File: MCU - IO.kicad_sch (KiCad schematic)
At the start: 1 part, among them U1 STM32H743ZIT6TR

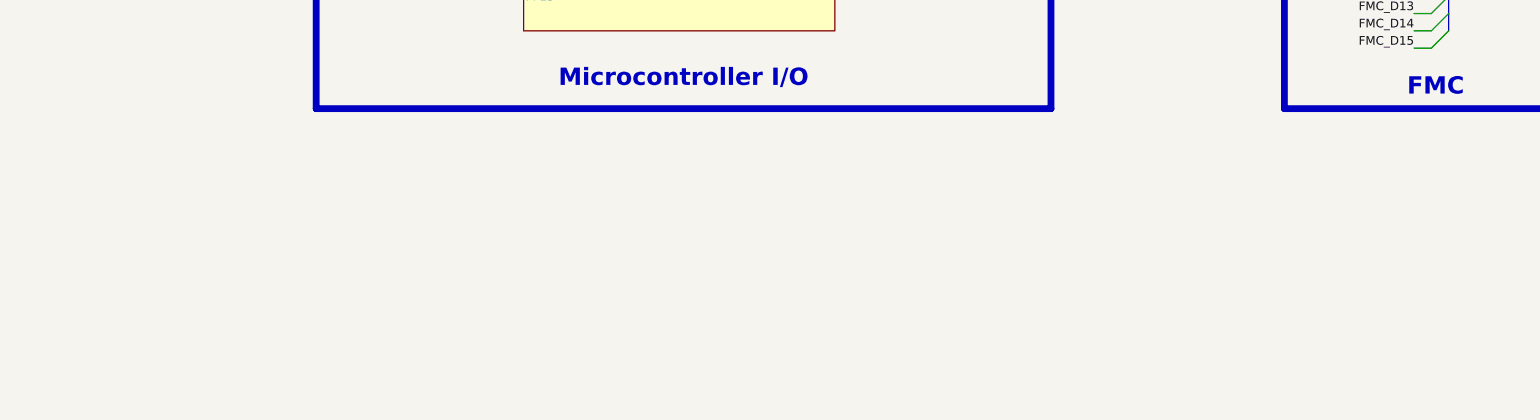
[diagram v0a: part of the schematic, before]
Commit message: added gas guage IC for monitoring battery
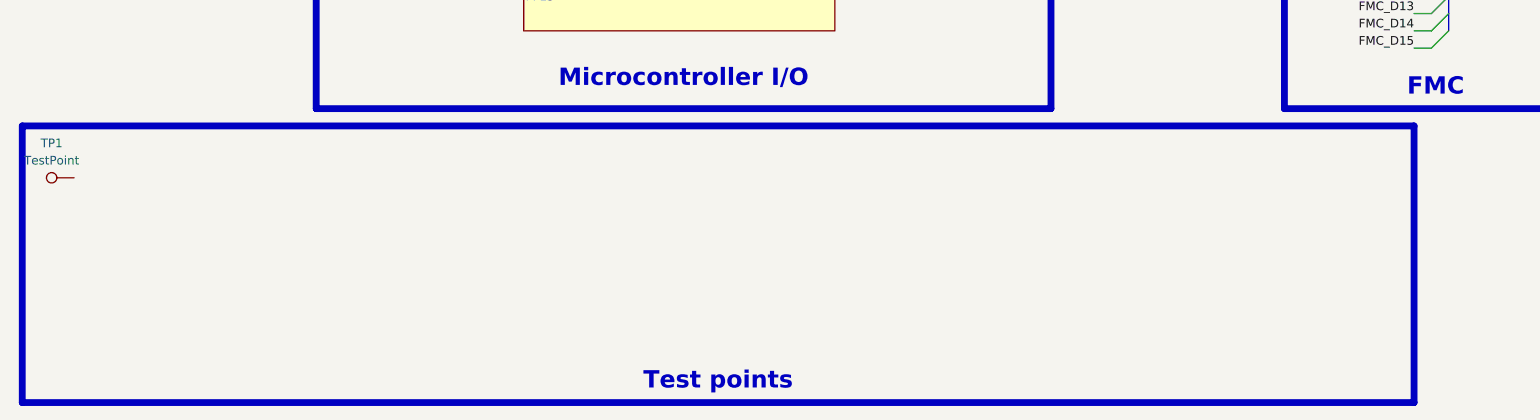
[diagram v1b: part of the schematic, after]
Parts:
- added TP1: TestPoint, symbol Connector:TestPoint
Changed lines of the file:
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@@
 	)
 	(rectangle
+		(start 13.97 243.84)
+		(end 218.44 284.48)
+		(stroke
+			(width 1)
+			(type default)
+			(color 200 200 200 1)
+		)
+		(fill
+			(type none)
+		)
+	)
+	(rectangle
 		(start 265.43 33.02)
 		(end 312.42 71.12)
@@
 		)
 	)
+	(text_box "Test points\n"
+		(exclude_from_sim no)
+		(at 13.97 271.78 0)
+		(size 204.47 12.7)
+		(margins 1.9049 1.9049 1.9049 1.9049)
+		(stroke
+			(width -0.0001)
+			(type solid)
+		)
+		(fill
+			(type none)
+		)
+		(effects
+			(font
+				(face "Times New Roman")
+				(size 2.54 2.54)
+				(thickness 0.508)
+				(bold yes)
+				(color 162 22 34 1)
+			)
+			(justify bottom)
+		)
+	)
 	(text_box "QUAD SPI\n"
 		(exclude_from_sim no)
@@
 				)
 			)
+		)
+	)
+	(symbol
+		(lib_id "Connector:TestPoint")
+		(at 21.59 251.46 90)
+		(unit 1)
+		(exclude_from_sim no)
+		(in_bom yes)
+		(on_board yes)
+		(dnp no)
+		(fields_autoplaced yes)
+		(property "Reference" "TP1"
+			(at 18.288 246.38 90)
+			(effects
+				(font
+					(size 1.27 1.27)
+				)
+			)
+		)
+		(property "Value" "TestPoint"
+			(at 18.288 248.92 90)
+			(effects
+				(font
+					(size 1.27 1.27)
+				)
+			)
+		)
+		(property "Footprint" ""
+			(at 21.59 246.38 0)
+			(effects
+				(font
+					(size 1.27 1.27)
+				)
+				(hide yes)
+			)
+		)
+		(property "Datasheet" "~"
+			(at 21.59 246.38 0)
+			(effects
+				(font
+					(size 1.27 1.27)
+				)
+				(hide yes)
+			)
+		)
+		(property "Description" "test point"
+			(at 21.59 251.46 0)
+			(effects
+				(font
+					(size 1.27 1.27)
+				)
+				(hide yes)
+			)
+		)
+		(pin "1"
+		)
+		(instances
+			(project ""
+				(path "/0650c7a8-acba-429c-9f8e-eec0baf0bc1c/fede4c36-00cc-4d3d-b71c-5243ba232202/e6015f1e-cbce-46f4-85e1-3d5463a17dc1"
+					(reference "TP1")
+					(unit 1)
+				)
+			)

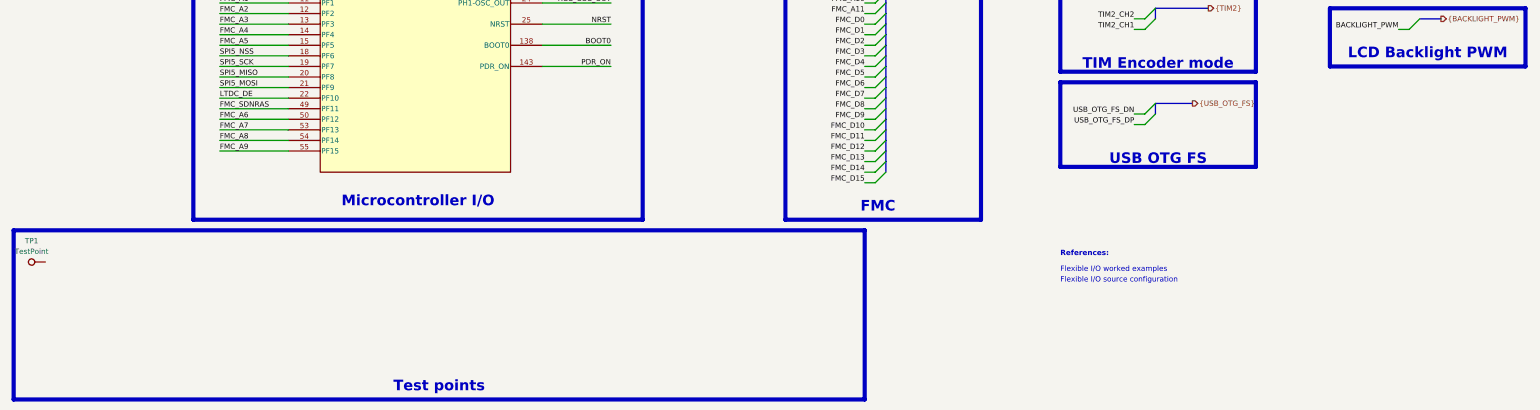
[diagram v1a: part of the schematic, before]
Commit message: added fiducal markers, mounting holes, testpoints
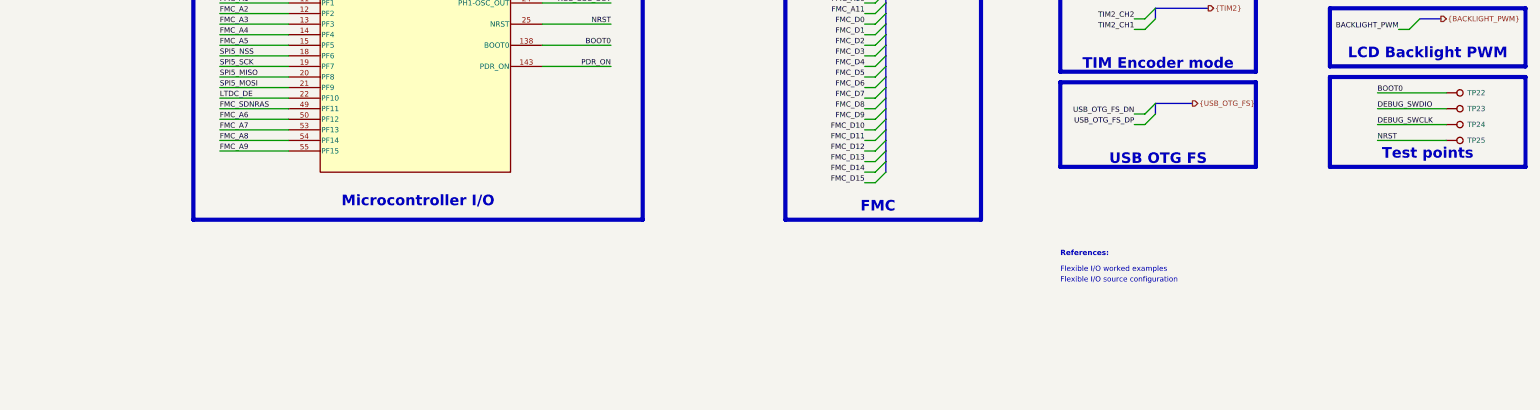
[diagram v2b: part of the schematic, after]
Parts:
- removed TP1: TestPoint, symbol Connector:TestPoint
- added TP22, TP23, TP24, TP25: TestPoint, 0_pads:TestPoint_Pad_D0.4mm_Back, symbol Connector:TestPoint
- U1: footprint LQFP-144_1_STM -> (none)
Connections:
- net BOOT0: now also TP22.1
- net DEBUG_SWCLK: now also TP24.1
- net DEBUG_SWDIO: now also TP23.1
- net NRST: now also TP25.1

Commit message: some visual changes, color of nets etc
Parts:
- U1: footprint (none) -> 0_integrated_circuits:LQFP-144_1_STM
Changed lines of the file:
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@@
 			)
 		)
-		(property "Footprint" ""
+		(property "Footprint" "0_integrated_circuits:LQFP-144_1_STM"
 			(at 80.01 45.72 0)
 			(effects
@@
 			)
 		)
-		(property "Footprint" ""
+		(property "Footprint" "0_integrated_circuits:LQFP-144_1_STM"
 			(at 80.01 143.51 0)
 			(effects

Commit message: test points, colors, drc
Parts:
- TP22, TP23, TP24, TP25: footprint 0_pads:TestPoint_Pad_D0.4mm_Back -> 0_pads:TestPoint_Pad_D0.5mm_Back
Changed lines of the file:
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@@
 			)
 		)
-		(property "Footprint" "0_pads:TestPoint_Pad_D0.4mm_Back"
+		(property "Footprint" "0_pads:TestPoint_Pad_D0.5mm_Back"
 			(at 358.14 223.52 0)
 			(effects
@@
 			)
 		)
-		(property "Footprint" "0_pads:TestPoint_Pad_D0.4mm_Back"
+		(property "Footprint" "0_pads:TestPoint_Pad_D0.5mm_Back"
 			(at 358.14 219.71 0)
 			(effects
@@
 			)
 		)
-		(property "Footprint" "0_pads:TestPoint_Pad_D0.4mm_Back"
+		(property "Footprint" "0_pads:TestPoint_Pad_D0.5mm_Back"
 			(at 358.14 227.33 0)
 			(effects
@@
 			)
 		)
-		(property "Footprint" "0_pads:TestPoint_Pad_D0.4mm_Back"
+		(property "Footprint" "0_pads:TestPoint_Pad_D0.5mm_Back"
 			(at 358.14 215.9 0)
 			(effects

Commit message: designator chagnes and cleanup silkscreen
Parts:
- U1: footprint 0_integrated_circuits:LQFP-144_1_STM -> LQFP-144_1_STM; LCSC PN (none) -> C114408
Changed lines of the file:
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@@
 			)
 		)
-		(property "Footprint" "0_integrated_circuits:LQFP-144_1_STM"
+		(property "Footprint" "LQFP-144_1_STM"
 			(at 80.01 45.72 0)
 			(effects
@@
 		)
 		(property "Supplier Part Number 1" "C114408"
+			(at 80.01 45.72 0)
+			(effects
+				(font
+					(size 1.27 1.27)
+				)
+				(hide yes)
+			)
+		)
+		(property "LCSC PN" "C114408"
 			(at 80.01 45.72 0)
 			(effects
@@
 			)
 		)
-		(property "Footprint" "0_integrated_circuits:LQFP-144_1_STM"
+		(property "Footprint" "LQFP-144_1_STM"
 			(at 80.01 143.51 0)
 			(effects
@@
 			(at 80.01 143.51 0)
 			(effects
+				(font
+					(size 1.27 1.27)
+				)
+				(hide yes)
+			)
+		)
+		(property "LCSC PN" "C114408"
+			(at 80.01 143.51 0)
+			(effects
